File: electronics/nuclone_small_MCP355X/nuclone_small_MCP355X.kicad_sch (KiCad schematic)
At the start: 54 parts, among them J3 nuclone_small_left, J4 nuclone_small_right, J5 FTDI_PINS_1X06, J6 DevBoardUartInput

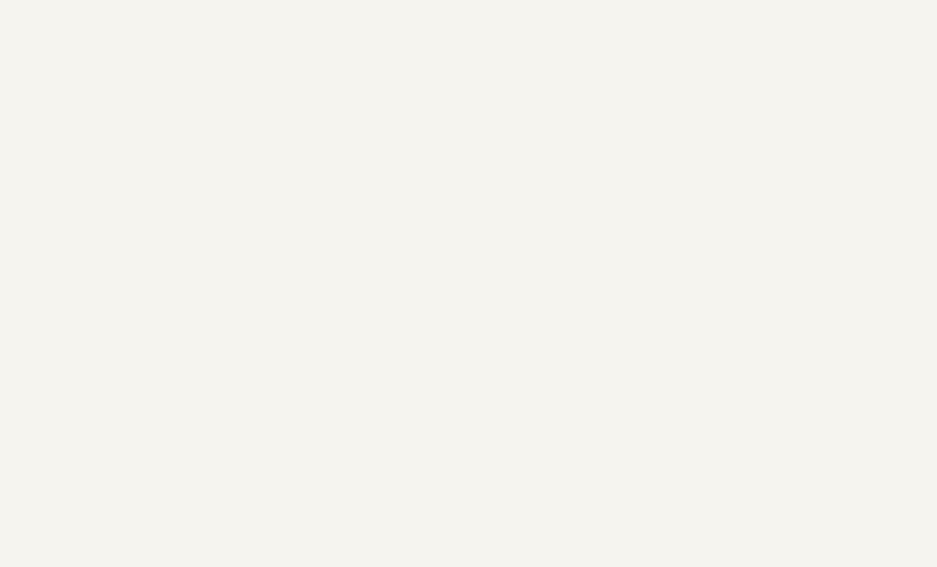
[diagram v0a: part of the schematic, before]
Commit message: WIP schematic entry
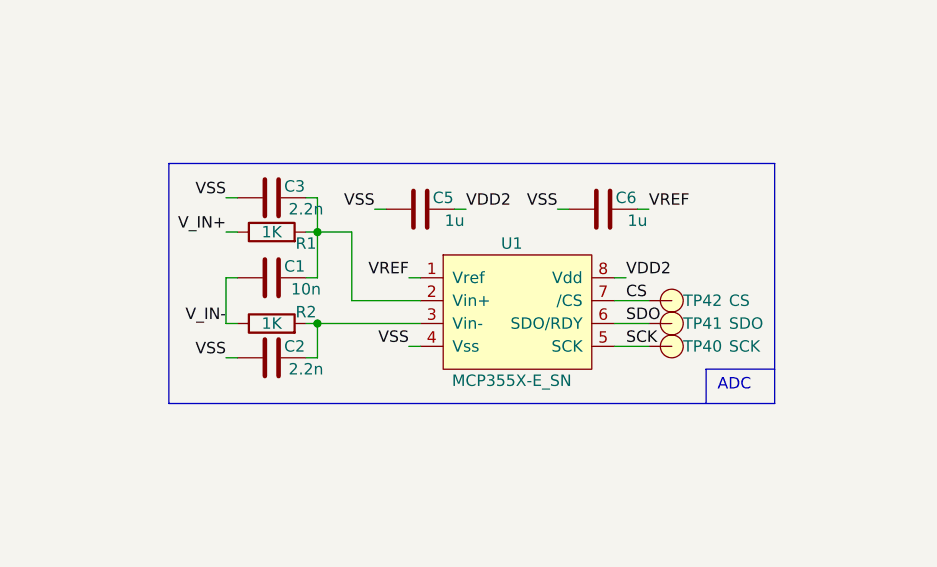
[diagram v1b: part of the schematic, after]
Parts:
- added C1: 10n, SquantorRcl:C_0603, symbol Device:C
- added C2, C3: 2.2n, SquantorRcl:C_0603, symbol Device:C
- added C5, C6: 1u, SquantorRcl:C_0603, symbol Device:C
- added R1, R2: 1K, SquantorRcl:R_0603_hand, symbol Device:R
- added TP40: SCK, SquantorTestPoints:TestPoint_hole_H05R10_2side, symbol SquantorProto:testpad
- added TP41: SDO, SquantorTestPoints:TestPoint_hole_H05R10_2side, symbol SquantorProto:testpad
- added TP42: CS, SquantorTestPoints:TestPoint_hole_H05R10_2side, symbol SquantorProto:testpad
- added U1: MCP355X-E_SN, symbol SquantorMicrochip:MCP355X-E_SN
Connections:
- net VDD2: now also C5.2, U1.8 (Vdd)
- net VSS: now also C2.1, C3.1, C5.1, C6.1, U1.4 (Vss)
- new net: C1.2, C3.2, R1.2, U1.2 (Vin+)
- new net: C2.2, R2.2, U1.3 (Vin-)
- new net CS: TP42.1, U1.7 (/CS)
- new net SCK: TP40.1, U1.5 (SCK)
- new net SDO: TP41.1, U1.6 (SDO/RDY)
- new net VREF: C6.2, U1.1 (Vref)
- new net V_IN+: R1.1
- new net V_IN-: C1.1, R2.1
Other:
- note added: "ADC"

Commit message: WIP schematic definition of MCP355X evaluator
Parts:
- added J1, J10, J11, J12, J2, J7, J8, J9: Conn_01x04, SquantorConnectors:Header-0254-1X04-H010, symbol Connector_Generic:Conn_01x04
- U1: footprint (none) -> SquantorIC:SOIC-8
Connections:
- net V_IN+: now also J2.1 (Pin_1), J2.2 (Pin_2), J2.3 (Pin_3), J2.4 (Pin_4)
- net V_IN-: now also J7.1 (Pin_1), J7.2 (Pin_2), J7.3 (Pin_3), J7.4 (Pin_4)
- new net Input1: J9.1 (Pin_1), J9.2 (Pin_2), J9.3 (Pin_3), J9.4 (Pin_4)
- new net Input2: J10.1 (Pin_1), J10.2 (Pin_2), J10.3 (Pin_3), J10.4 (Pin_4)
- new net Input3: J11.1 (Pin_1), J11.2 (Pin_2), J11.3 (Pin_3), J11.4 (Pin_4)
- new net Input4: J12.1 (Pin_1), J12.2 (Pin_2), J12.3 (Pin_3), J12.4 (Pin_4)
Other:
- note added: "Breadboard"
- moved on the sheet: C1, C2, C3, C5, C6, R1, R2, TP40, TP41, TP42, U1

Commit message: WIP schematic, added breadboard, initial placement
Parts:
- added D2, D3, D4, D5: SD05, SquantorDiodes:SOD-323-nexperia-hand, symbol Device:D_TVS
- added J13: Conn_01x04, Connector_JST:JST_XH_B4B-XH-A_1x04_P2.50mm_Vertical, symbol Connector_Generic:Conn_01x04
- added R10, R11, R4, R5, R6, R7, R8, R9: 1K, SquantorRcl:R_0805+0603, symbol Device:R
- added R3: 100, SquantorRcl:R_0603_hand, symbol Device:R
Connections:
- net Input1: now also D2.1 (A1), J13.1 (Pin_1)
- net Input2: now also D3.1 (A1), J13.2 (Pin_2)
- net Input3: now also D4.1 (A1), J13.3 (Pin_3)
- net Input4: now also D5.1 (A1), J13.4 (Pin_4)
- net VDD2: now also R3.2; no longer C5.2, U1.8 (Vdd)
- net VREF: now also R11.2, R5.2, R7.2, R9.2
- net VSS: now also D2.2 (A2), D3.2 (A2), D4.2 (A2), D5.2 (A2), R10.2, R4.2, R6.2, R8.2
- net DIV3: now reaches J8.1 (Pin_1)
- net DIV3: now also J8.2 (Pin_2), R8.1, R9.1
- net DIV4: now reaches J8.3 (Pin_3)
- net DIV4: now also J8.4 (Pin_4), R10.1, R11.1
- net DIV1: now reaches J1.1 (Pin_1)
- net DIV1: now also J1.2 (Pin_2), R4.1, R5.1
- net DIV2: now reaches J1.3 (Pin_3)
- net DIV2: now also J1.4 (Pin_4), R6.1, R7.1
- new net: C5.2, R3.1, U1.8 (Vdd)
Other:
- note added: "Dividers"
- note added: "Input connection"
- moved on the sheet: C6

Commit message: placing and silk placement
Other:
- note added: "Voltage reference"
- note removed: "MCP355X with reference"
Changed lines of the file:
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@@
     (stroke (width 0) (type default))
-  )
-  (text "MCP355X with reference" (at 109.22 168.91 0)
-    (effects (font (size 1.27 1.27)) (justify left bottom))
   )
   (text "Labels and mounting" (at 34.29 193.04 0)
     (effects (font (size 1.27 1.27)) (justify left bottom))
   )
+  (text "Voltage reference" (at 107.95 168.91 0)
+    (effects (font (size 1.27 1.27)) (justify left bottom))
+  )

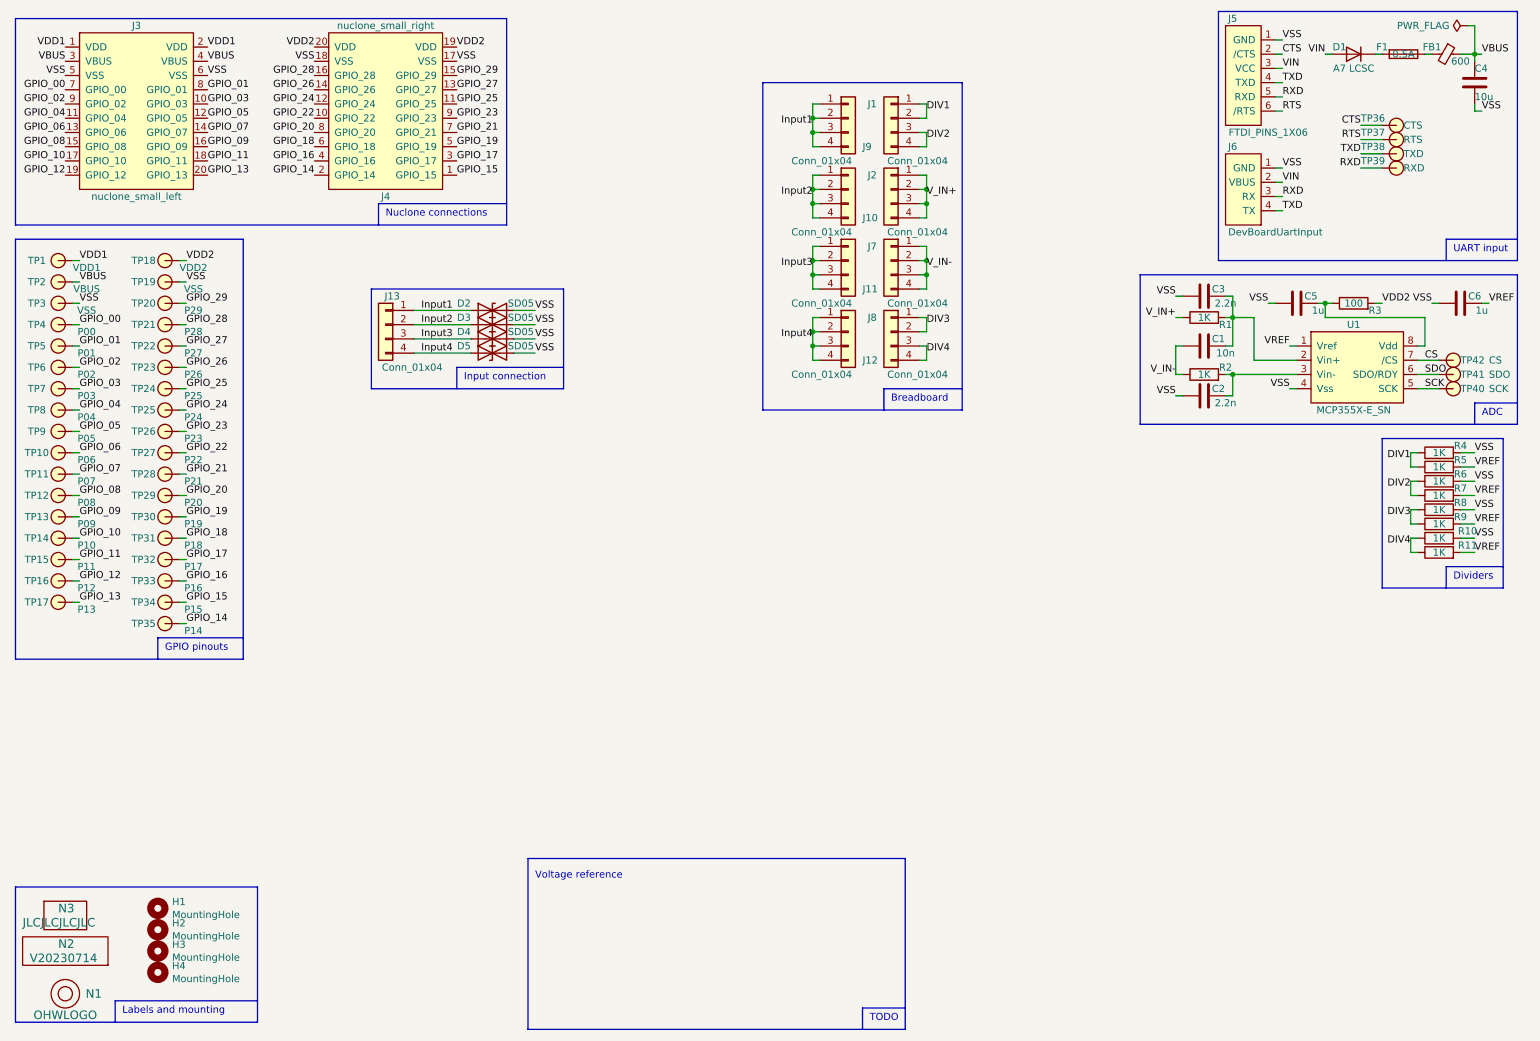
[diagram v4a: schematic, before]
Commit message: added Voltage reference, placed and routed
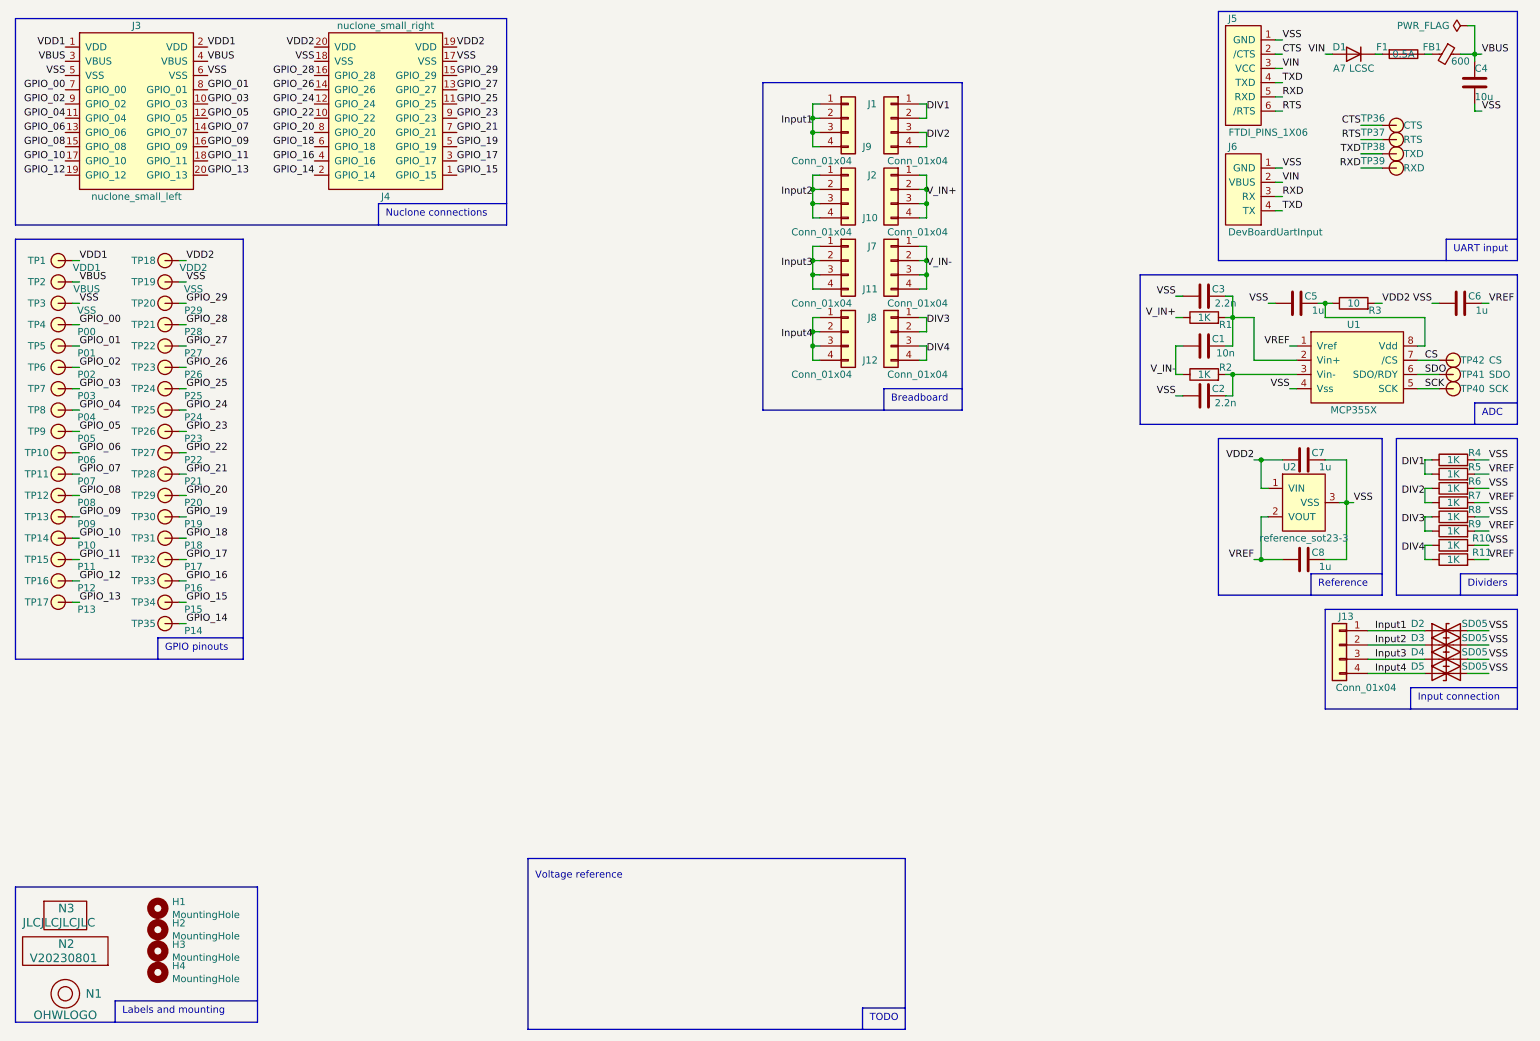
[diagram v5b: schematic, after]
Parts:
- added C7, C8: 1u, SquantorRcl:C_0603, symbol Device:C
- added U2: reference_sot23-3, SquantorIC:SOT23-3, symbol SquantorGenericAnalog:reference_sot23-3
- N2: value V20230714 -> V20230801
- R3: value 100 -> 10
- U1: value MCP355X-E_SN -> MCP355X
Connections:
- net VDD2: now also C7.1, U2.1 (VIN)
- net VREF: now also C8.1, U2.2 (VOUT)
- net VSS: now also C7.2, C8.2, U2.3 (VSS)
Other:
- note added: "Reference"
- moved on the sheet: D2, D3, D4, D5, J13, R10, R11, R4, R5, R6, R7, R8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

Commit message: reviewed and small modifications
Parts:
- removed TP40: SCK, SquantorTestPoints:TestPoint_hole_H05R10_2side, symbol SquantorProto:testpad
- removed TP41: SDO, SquantorTestPoints:TestPoint_hole_H05R10_2side, symbol SquantorProto:testpad
- removed TP42: CS, SquantorTestPoints:TestPoint_hole_H05R10_2side, symbol SquantorProto:testpad
- added J14: Conn_01x03, SquantorConnectors:Header-0254-1X03-H010, symbol Connector_Generic:Conn_01x03
- N2: value V20230801 -> V20230915
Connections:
- net CS: now also J14.1 (Pin_1)
- net SCK: now also J14.3 (Pin_3)
- net SDO: now also J14.2 (Pin_2)
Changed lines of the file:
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@@
       (effects (font (size 1.524 1.524)) (justify left))
     )
-    (property "Value" "V20230801" (at 17.78 182.88 0)
+    (property "Value" "V20230915" (at 17.78 182.88 0)
       (effects (font (size 1.524 1.524)) (justify left))
     )
@@
     )
   )
-  (symbol (lib_id "SquantorProto:testpad") (at 271.78 76.2 0) (unit 1)
-    (in_bom yes) (on_board yes) (dnp no)
-    (property "Reference" "TP42" (at 273.05 76.2 0)
-      (effects (font (size 1.27 1.27)) (justify left))
-    )
-    (property "Value" "CS" (at 278.13 76.2 0)
-      (effects (font (size 1.27 1.27)) (justify left))
-    )
-    (property "Footprint" "SquantorTestPoints:TestPoint_hole_H05R10_2side" (at 273.05 75.565 0)
-      (effects (font (size 1.27 1.27)) hide)
-    )
-    (property "Datasheet" "" (at 273.05 75.565 0)
-      (effects (font (size 1.27 1.27)) hide)
-    )
-    (pin "1")
-    (instances
-      (project "nuclone_small_MCP355X"
-        (path "/917603e2-441d-4888-a037-0b830871fafd"
-          (reference "TP42") (unit 1)
-        )
-      )
-    )
-  )
   (symbol (lib_id "Device:R") (at 271.78 93.98 90) (unit 1)
     (in_bom yes) (on_board yes) (dnp no)
@@
     )
   )
-  (symbol (lib_id "SquantorProto:testpad") (at 271.78 78.74 0) (unit 1)
-    (in_bom yes) (on_board yes) (dnp no)
-    (property "Reference" "TP41" (at 273.05 78.74 0)
-      (effects (font (size 1.27 1.27)) (justify left))
-    )
-    (property "Value" "SDO" (at 278.13 78.74 0)
-      (effects (font (size 1.27 1.27)) (justify left))
-    )
-    (property "Footprint" "SquantorTestPoints:TestPoint_hole_H05R10_2side" (at 273.05 78.105 0)
-      (effects (font (size 1.27 1.27)) hide)
-    )
-    (property "Datasheet" "" (at 273.05 78.105 0)
-      (effects (font (size 1.27 1.27)) hide)
-    )
-    (pin "1")
-    (instances
-      (project "nuclone_small_MCP355X"
-        (path "/917603e2-441d-4888-a037-0b830871fafd"
-          (reference "TP41") (unit 1)
-        )
-      )
-    )
-  )
   (symbol (lib_id "Device:D_TVS") (at 270.51 124.46 0) (unit 1)
     (in_bom yes) (on_board yes) (dnp no)
@@
         (path "/917603e2-441d-4888-a037-0b830871fafd"
           (reference "J2") (unit 1)
+        )
+      )
+    )
+  )
+  (symbol (lib_id "Connector_Generic:Conn_01x03") (at 274.32 78.74 0) (unit 1)
+    (in_bom yes) (on_board yes) (dnp no)
+    (property "Reference" "J14" (at 271.78 73.66 0)
+      (effects (font (size 1.27 1.27)) (justify left))
+    )
+    (property "Value" "Conn_01x03" (at 276.86 80.01 0)
+      (effects (font (size 1.27 1.27)) (justify left) hide)
+    )
+    (property "Footprint" "SquantorConnectors:Header-0254-1X03-H010" (at 274.32 78.74 0)
+      (effects (font (size 1.27 1.27)) hide)
+    )
+    (property "Datasheet" "~" (at 274.32 78.74 0)
+      (effects (font (size 1.27 1.27)) hide)
+    )
+    (pin "1")
+    (pin "2")
+    (pin "3")
+    (instances
+      (project "nuclone_small_MCP355X"
+        (path "/917603e2-441d-4888-a037-0b830871fafd"
+          (reference "J14") (unit 1)
         )
       )
@@
         )
       )
-    )
-  )
-  (symbol (lib_id "SquantorProto:testpad") (at 271.78 81.28 0) (unit 1)
-    (in_bom yes) (on_board yes) (dnp no)
-    (property "Reference" "TP40" (at 273.05 81.28 0)
-      (effects (font (size 1.27 1.27)) (justify left))
-    )
-    (property "Value" "SCK" (at 278.13 81.28 0)
-      (effects (font (size 1.27 1.27)) (justify left))
-    )
-    (property "Footprint" "SquantorTestPoints:TestPoint_hole_H05R10_2side" (at 273.05 80.645 0)
-      (effects (font (size 1.27 1.27)) hide)
-    )
-    (property "Datasheet" "" (at 273.05 80.645 0)
-      (effects (font (size 1.27 1.27)) hide)
-    )
-    (pin "1")
-    (instances
-      (project "nuclone_small_MCP355X"
-        (path "/917603e2-441d-4888-a037-0b830871fafd"
-          (reference "TP40") (unit 1)
-        )
-      )

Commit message: updated changes and library
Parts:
- removed J14: Conn_01x03, SquantorConnectors:Header-0254-1X03-H010, symbol Connector_Generic:Conn_01x03
- removed J5: FTDI_PINS_1X06, SquantorConnectors:Header-0254-1X06-H010, symbol SquantorConnectorsNamed:FTDI_PINS_1X06
- removed TP36: CTS, SquantorTestPoints:TestPoint_hole_H05R10_2side, symbol SquantorProto:testpad
- removed TP37: RTS, SquantorTestPoints:TestPoint_hole_H05R10_2side, symbol SquantorProto:testpad
- removed TP38: TXD, SquantorTestPoints:TestPoint_hole_H05R10_2side, symbol SquantorProto:testpad
- removed TP39: RXD, SquantorTestPoints:TestPoint_hole_H05R10_2side, symbol SquantorProto:testpad
- added D6: LED, SquantorDiodes:LED_0603_hand, symbol Device:LED
- added J15: Conn_02x03_Odd_Even, SquantorConnectors:Header-0254-2X03-H010, symbol Connector_Generic:Conn_02x03_Odd_Even
- added J16: Conn_02x04_Odd_Even, SquantorConnectors:Header-0254-2X04-H010, symbol Connector_Generic:Conn_02x04_Odd_Even
- added R12: 1K, SquantorRcl:R_0603_hand, symbol Device:R
- J10, J11, J12, J9: footprint SquantorConnectors:Header-0254-1X04-H010 -> SquantorConnectors:Header-0254-1X02-H010; symbol Connector_Generic:Conn_01x04 -> Connector_Generic:Conn_01x02
- N2: value V20230915 -> V20231203
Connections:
- net CS: now also J15.1 (Pin_1)
- net Input1: no longer J9.3 (Pin_3), J9.4 (Pin_4)
- net Input2: no longer J10.3 (Pin_3), J10.4 (Pin_4)
- net Input3: no longer J11.3 (Pin_3), J11.4 (Pin_4)
- net Input4: no longer J12.3 (Pin_3), J12.4 (Pin_4)
- net RXD: now also J16.7 (Pin_7)
- net SCK: now also J15.5 (Pin_5)
- net SDO: now also J15.3 (Pin_3)
- net TXD: now also J16.5 (Pin_5)
- net VBUS: now also R12.2
- net VSS: now also D6.1 (K), J15.2 (Pin_2), J15.4 (Pin_4), J15.6 (Pin_6), J16.2 (Pin_2), J16.4 (Pin_4), J16.6 (Pin_6), J16.8 (Pin_8)
- new net: D6.2 (A), R12.1
- no-connect marks 0 -> 2
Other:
- moved on the sheet: C1, C2, C3, C4, C5, C6, D1, F1, FB1, J1, J2, J6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
